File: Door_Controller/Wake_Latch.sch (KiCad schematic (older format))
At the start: 21 parts

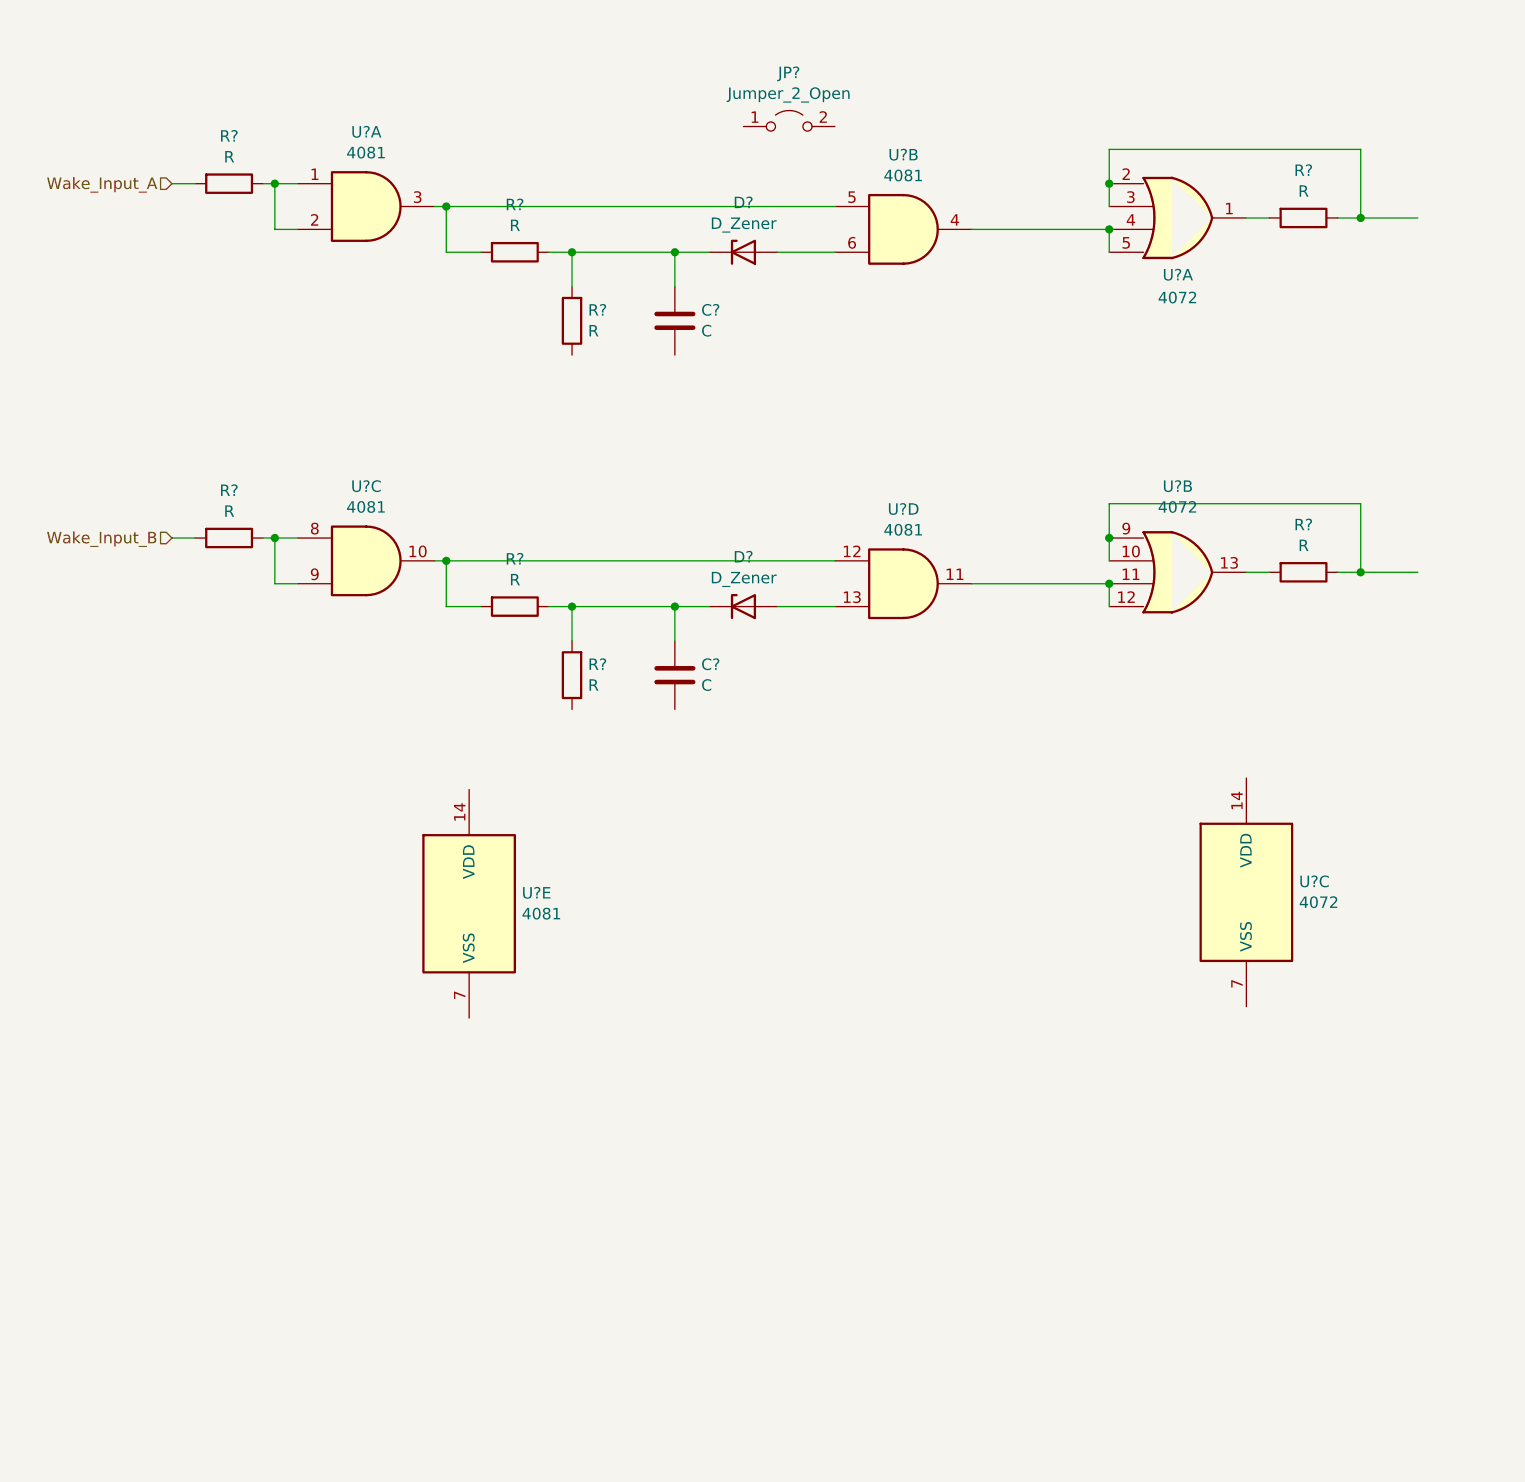
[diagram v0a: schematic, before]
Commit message: complete wake-latch subsheet
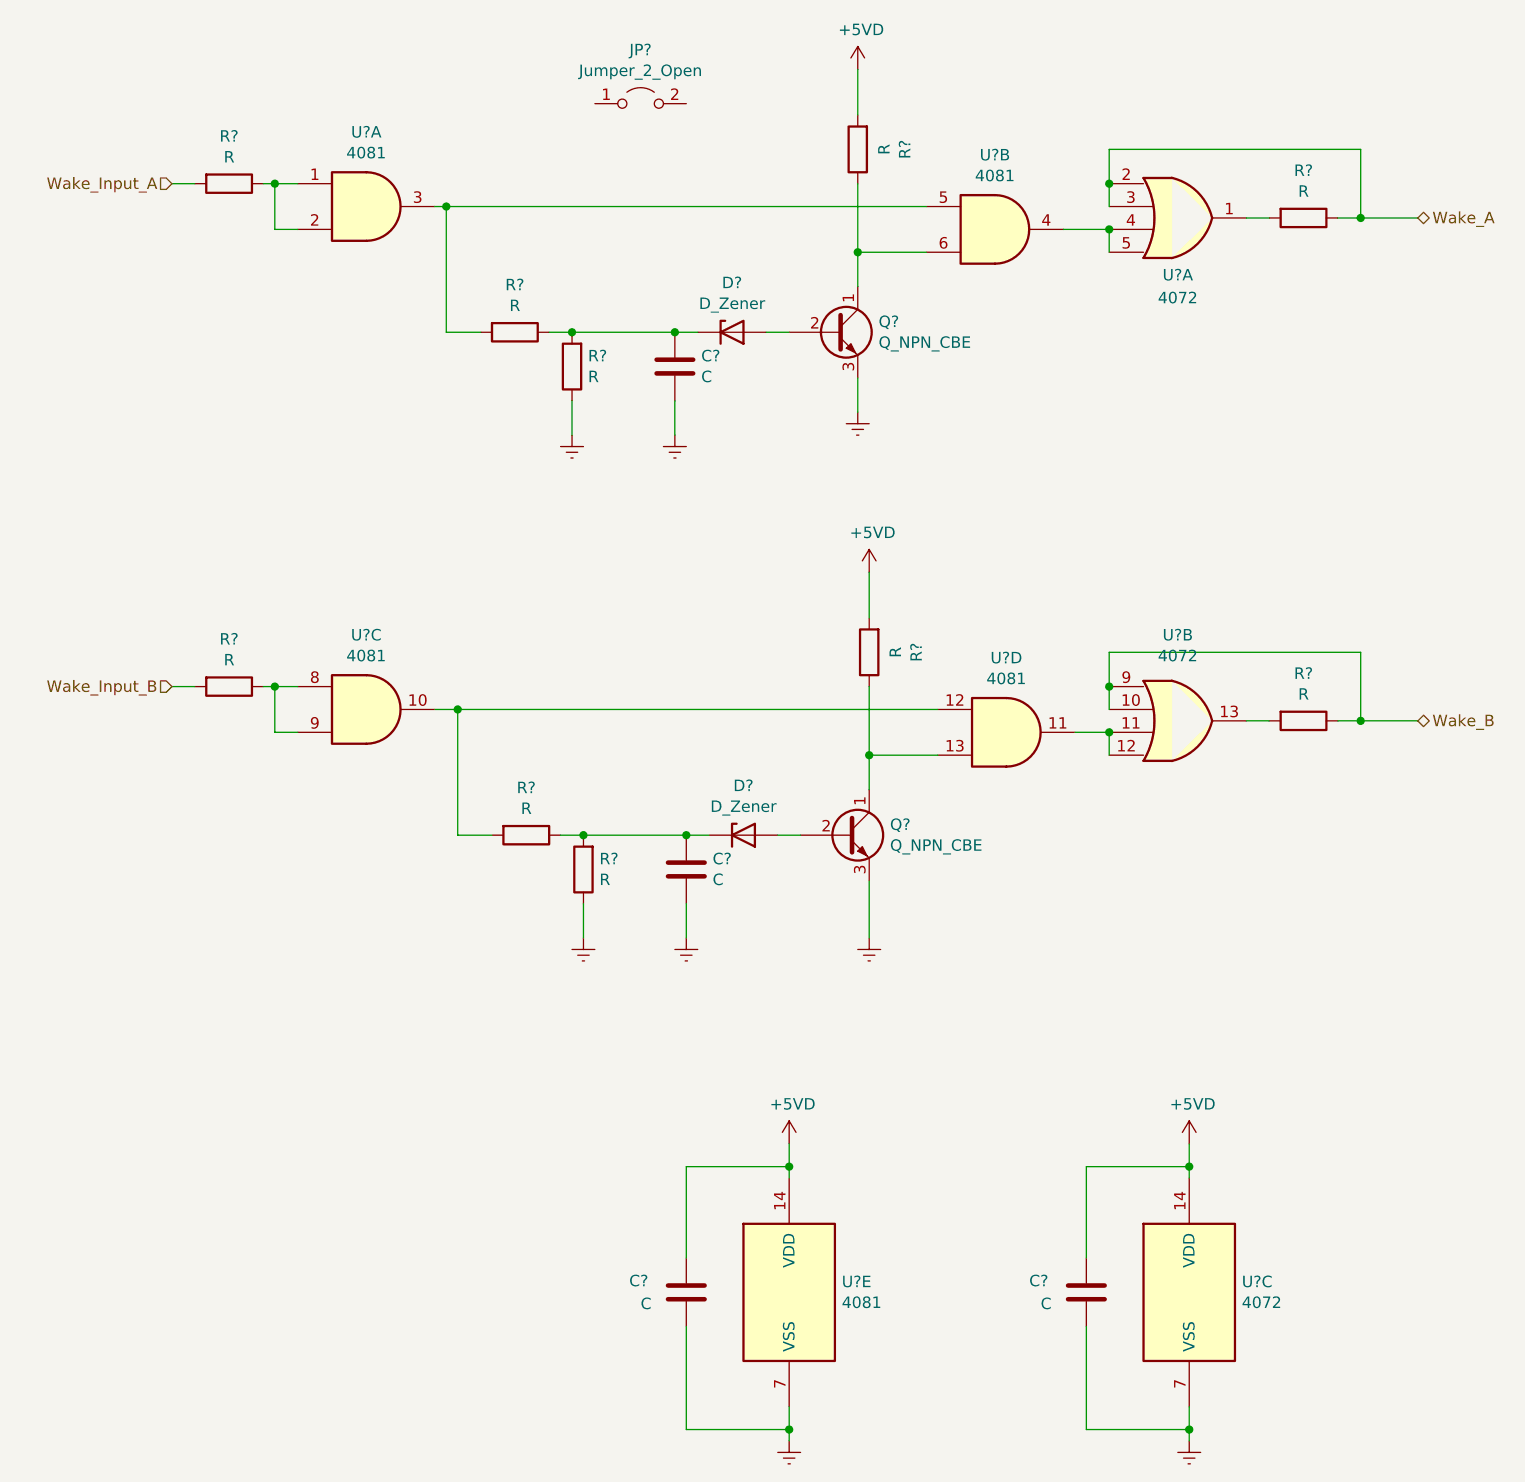
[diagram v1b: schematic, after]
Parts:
- removed C?: C, symbol Device:C
- removed D?: D_Zener, symbol Device:D_Zener
- removed R? (x2): R, symbol Device:R
- added C? (x3): C, symbol Device:C
- added D?: D_Zener, symbol Device:D_Zener
- added Q? (x2): Q_NPN_CBE, symbol Device:Q_NPN_CBE
- added R? (x4): R, symbol Device:R
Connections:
- net labels added: +5VD, Earth, Wake_A, Wake_B
- wire segments 48 -> 74
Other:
- moved on the sheet: C?, D?, JP?, R?, U?B, U?C, U?D, U?E

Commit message: simplified wake disable
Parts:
- removed JP?: Jumper_2_Open, symbol Jumper:Jumper_2_Open
- removed R? (x2): R, symbol Device:R
- R? (x2): value R -> 100
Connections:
- net Wake_A: now also U?.1; no longer U?.2, U?.3
- net Wake_B: now also U?.13; no longer U?.10, U?.9
- no-connect marks 0 -> 4
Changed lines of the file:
@@
 AR Path="/60BD8BC8/613ABD4B/60BF2346" Ref="R?"  Part="1"
 AR Path="/60BD8BC8/613AC461/60BF2346" Ref="R?"  Part="1"
-F 0 "R?" V 1343 1850 50  0000 C CNN
-F 1 "R" V 1434 1850 50  0000 C CNN
+F 0 "R?" V 1450 1850 50  0000 C CNN
+F 1 "100" V 1550 1850 50  0000 C CNN
 F 2 "" V 1480 1850 50  0001 C CNN
 F 3 "~" H 1550 1850 50  0001 C CNN
@@
 AR Path="/60BD8BC8/613ABD4B/60C15BD1" Ref="R?"  Part="1"
 AR Path="/60BD8BC8/613AC461/60C15BD1" Ref="R?"  Part="1"
-F 0 "R?" V 1343 4050 50  0000 C CNN
-F 1 "R" V 1434 4050 50  0000 C CNN
+F 0 "R?" V 1450 4050 50  0000 C CNN
+F 1 "100" V 1550 4050 50  0000 C CNN
 F 2 "" V 1480 4050 50  0001 C CNN
 F 3 "~" H 1550 4050 50  0001 C CNN
@@
 Wire Wire Line
 	1750 4050 1850 4050
-$Comp
-L Device:R R?
-U 1 1 60C216FA
-P 6250 4200
-AR Path="/60BD8BC8/60BD8C71/60C216FA" Ref="R?"  Part="1"
-AR Path="/60BD8BC8/613ABD4B/60C216FA" Ref="R?"  Part="1"
-AR Path="/60BD8BC8/613AC461/60C216FA" Ref="R?"  Part="1"
-F 0 "R?" V 6043 4200 50  0000 C CNN
-F 1 "R" V 6134 4200 50  0000 C CNN
-F 2 "" V 6180 4200 50  0001 C CNN
-F 3 "~" H 6250 4200 50  0001 C CNN
-	1    6250 4200
-	0    1    1    0
-$EndComp
-Wire Wire Line
-	6000 4200 6100 4200
-Wire Wire Line
-	6400 4200 6500 4200
-Wire Wire Line
-	6500 4200 6500 3900
-Wire Wire Line
-	6500 3900 5400 3900
-Connection ~ 6500 4200
-Wire Wire Line
-	6500 4200 6750 4200
-Wire Wire Line
-	5400 3900 5400 4050
-Wire Wire Line
-	5400 4050 5400 4150
-Connection ~ 5400 4050
 Wire Wire Line
 	5400 4250 5400 4350
@@
 	5400 4250 5250 4250
 Connection ~ 5400 4250
-$Comp
-L Jumper:Jumper_2_Open JP?
-U 1 1 60BECC23
-P 3350 1500
-AR Path="/60BD8BC8/60BD8C71/60BECC23" Ref="JP?"  Part="1"
-AR Path="/60BD8BC8/613ABD4B/60BECC23" Ref="JP?"  Part="1"
-AR Path="/60BD8BC8/613AC461/60BECC23" Ref="JP?"  Part="1"
-F 0 "JP?" H 3350 1735 50  0000 C CNN
-F 1 "Jumper_2_Open" H 3350 1644 50  0000 C CNN
-F 2 "" H 3350 1500 50  0001 C CNN
-F 3 "~" H 3350 1500 50  0001 C CNN
-	1    3350 1500
-	1    0    0    -1
-$EndComp
-Wire Wire Line
-	6500 2000 6750 2000
-Connection ~ 6500 2000
-Wire Wire Line
-	6500 2000 6500 1700
-Wire Wire Line
-	6000 2000 6100 2000
-$Comp
-L Device:R R?
-U 1 1 60C04CFC
-P 6250 2000
-AR Path="/60BD8BC8/60BD8C71/60C04CFC" Ref="R?"  Part="1"
-AR Path="/60BD8BC8/613ABD4B/60C04CFC" Ref="R?"  Part="1"
-AR Path="/60BD8BC8/613AC461/60C04CFC" Ref="R?"  Part="1"
-F 0 "R?" V 6043 2000 50  0000 C CNN
-F 1 "R" V 6134 2000 50  0000 C CNN
-F 2 "" V 6180 2000 50  0001 C CNN
-F 3 "~" H 6250 2000 50  0001 C CNN
-	1    6250 2000
-	0    1    1    0
-$EndComp
-Connection ~ 5400 1850
-Wire Wire Line
-	5400 1700 5400 1850
-Wire Wire Line
-	5400 1950 5400 1850
 Connection ~ 5400 2050
 Wire Wire Line
@@
 $EndComp
 Wire Wire Line
-	6400 2000 6500 2000
-Wire Wire Line
-	6500 1700 5400 1700
-Wire Wire Line
 	5200 2050 5400 2050
 $Comp
@@
 AR Path="/60BD8BC8/613ABD4B/6134AFF9" Ref="R?"  Part="1"
 AR Path="/60BD8BC8/613AC461/6134AFF9" Ref="R?"  Part="1"
-F 0 "R?" V 4093 1700 50  0000 C CNN
-F 1 "R" V 4184 1700 50  0000 C CNN
+F 0 "R?" V 4200 1700 50  0000 C CNN
+F 1 "R" V 4300 1700 50  0000 C CNN
 F 2 "" V 4230 1700 50  0001 C CNN
 F 3 "~" H 4300 1700 50  0001 C CNN
@@
 AR Path="/60BD8BC8/613ABD4B/61358B50" Ref="R?"  Part="1"
 AR Path="/60BD8BC8/613AC461/61358B50" Ref="R?"  Part="1"
-F 0 "R?" V 4143 3900 50  0000 C CNN
-F 1 "R" V 4234 3900 50  0000 C CNN
+F 0 "R?" V 4250 3900 50  0000 C CNN
+F 1 "R" V 4350 3900 50  0000 C CNN
 F 2 "" V 4280 3900 50  0001 C CNN
 F 3 "~" H 4350 3900 50  0001 C CNN
@@
 AR Path="/60BD8BC8/613ABD4B/60BF7A25" Ref="R?"  Part="1"
 AR Path="/60BD8BC8/613AC461/60BF7A25" Ref="R?"  Part="1"
-F 0 "R?" H 2980 2604 50  0000 R CNN
-F 1 "R" H 2980 2695 50  0000 R CNN
+F 0 "R?" V 2950 2700 50  0000 R CNN
+F 1 "R" V 3050 2700 50  0000 R CNN
 F 2 "" V 2980 2650 50  0001 C CNN
 F 3 "~" H 3050 2650 50  0001 C CNN
@@
 AR Path="/60BD8BC8/613ABD4B/60BF7586" Ref="R?"  Part="1"
 AR Path="/60BD8BC8/613AC461/60BF7586" Ref="R?"  Part="1"
-F 0 "R?" V 2593 2500 50  0000 C CNN
-F 1 "R" V 2684 2500 50  0000 C CNN
+F 0 "R?" V 2700 2500 50  0000 C CNN
+F 1 "R" V 2800 2500 50  0000 C CNN
 F 2 "" V 2730 2500 50  0001 C CNN
 F 3 "~" H 2800 2500 50  0001 C CNN
@@
 AR Path="/60BD8BC8/613ABD4B/613638AF" Ref="R?"  Part="1"
 AR Path="/60BD8BC8/613AC461/613638AF" Ref="R?"  Part="1"
-F 0 "R?" H 3030 4804 50  0000 R CNN
-F 1 "R" H 3030 4895 50  0000 R CNN
+F 0 "R?" V 3000 4900 50  0000 R CNN
+F 1 "R" V 3100 4900 50  0000 R CNN
 F 2 "" V 3030 4850 50  0001 C CNN
 F 3 "~" H 3100 4850 50  0001 C CNN
@@
 AR Path="/60BD8BC8/613ABD4B/613638B9" Ref="R?"  Part="1"
 AR Path="/60BD8BC8/613AC461/613638B9" Ref="R?"  Part="1"
-F 0 "R?" V 2643 4700 50  0000 C CNN
-F 1 "R" V 2734 4700 50  0000 C CNN
+F 0 "R?" V 2750 4700 50  0000 C CNN
+F 1 "R" V 2850 4700 50  0000 C CNN
 F 2 "" V 2780 4700 50  0001 C CNN
 F 3 "~" H 2850 4700 50  0001 C CNN
@@
 Text HLabel 6750 4200 2    50   BiDi ~ 0
 Wake_B
+Wire Wire Line
+	6000 2000 6750 2000
+NoConn ~ 5400 1850
+NoConn ~ 5400 1950
+NoConn ~ 5400 4050
+NoConn ~ 5400 4150
+Wire Wire Line
+	6000 4200 6750 4200
 $EndSCHEMATC

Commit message: specify wake pulse circuit to ltspice model
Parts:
- C? (x2): value C -> 220nF
- D? (x2): value D_Zener -> 4.7V
- R? (x4): value R -> 100K
- R? (x2): value R -> 1M
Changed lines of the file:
@@
 AR Path="/60BD8BC8/613AC461/6134AFF9" Ref="R?"  Part="1"
 F 0 "R?" V 4200 1700 50  0000 C CNN
-F 1 "R" V 4300 1700 50  0000 C CNN
+F 1 "100K" V 4300 1700 50  0000 C CNN
 F 2 "" V 4230 1700 50  0001 C CNN
 F 3 "~" H 4300 1700 50  0001 C CNN
@@
 AR Path="/60BD8BC8/613AC461/61358B50" Ref="R?"  Part="1"
 F 0 "R?" V 4250 3900 50  0000 C CNN
-F 1 "R" V 4350 3900 50  0000 C CNN
+F 1 "100K" V 4350 3900 50  0000 C CNN
 F 2 "" V 4280 3900 50  0001 C CNN
 F 3 "~" H 4350 3900 50  0001 C CNN
@@
 AR Path="/60BD8BC8/613AC461/60BFAC12" Ref="D?"  Part="1"
 F 0 "D?" H 3750 2716 50  0000 C CNN
-F 1 "D_Zener" H 3750 2625 50  0000 C CNN
+F 1 "4.7V" H 3750 2625 50  0000 C CNN
 F 2 "" H 3750 2500 50  0001 C CNN
 F 3 "~" H 3750 2500 50  0001 C CNN
@@
 AR Path="/60BD8BC8/613AC461/60BF9FE4" Ref="C?"  Part="1"
 F 0 "C?" H 3615 2696 50  0000 L CNN
-F 1 "C" H 3615 2605 50  0000 L CNN
+F 1 "220nF" H 3615 2605 50  0000 L CNN
 F 2 "" H 3538 2500 50  0001 C CNN
 F 3 "~" H 3500 2650 50  0001 C CNN
@@
 AR Path="/60BD8BC8/613AC461/60BF7A25" Ref="R?"  Part="1"
 F 0 "R?" V 2950 2700 50  0000 R CNN
-F 1 "R" V 3050 2700 50  0000 R CNN
+F 1 "1M" V 3050 2700 50  0000 R CNN
 F 2 "" V 2980 2650 50  0001 C CNN
 F 3 "~" H 3050 2650 50  0001 C CNN
@@
 AR Path="/60BD8BC8/613AC461/60BF7586" Ref="R?"  Part="1"
 F 0 "R?" V 2700 2500 50  0000 C CNN
-F 1 "R" V 2800 2500 50  0000 C CNN
+F 1 "100K" V 2800 2500 50  0000 C CNN
 F 2 "" V 2730 2500 50  0001 C CNN
 F 3 "~" H 2800 2500 50  0001 C CNN
@@
 AR Path="/60BD8BC8/613AC461/6136389B" Ref="D?"  Part="1"
 F 0 "D?" H 3800 4916 50  0000 C CNN
-F 1 "D_Zener" H 3800 4825 50  0000 C CNN
+F 1 "4.7V" H 3800 4825 50  0000 C CNN
 F 2 "" H 3800 4700 50  0001 C CNN
 F 3 "~" H 3800 4700 50  0001 C CNN
@@
 AR Path="/60BD8BC8/613AC461/613638A5" Ref="C?"  Part="1"
 F 0 "C?" H 3665 4896 50  0000 L CNN
-F 1 "C" H 3665 4805 50  0000 L CNN
+F 1 "220nF" H 3665 4805 50  0000 L CNN
 F 2 "" H 3588 4700 50  0001 C CNN
 F 3 "~" H 3550 4850 50  0001 C CNN
@@
 AR Path="/60BD8BC8/613AC461/613638AF" Ref="R?"  Part="1"
 F 0 "R?" V 3000 4900 50  0000 R CNN
-F 1 "R" V 3100 4900 50  0000 R CNN
+F 1 "1M" V 3100 4900 50  0000 R CNN
 F 2 "" V 3030 4850 50  0001 C CNN
 F 3 "~" H 3100 4850 50  0001 C CNN
@@
 AR Path="/60BD8BC8/613AC461/613638B9" Ref="R?"  Part="1"
 F 0 "R?" V 2750 4700 50  0000 C CNN
-F 1 "R" V 2850 4700 50  0000 C CNN
+F 1 "100K" V 2850 4700 50  0000 C CNN
 F 2 "" V 2780 4700 50  0001 C CNN
 F 3 "~" H 2850 4700 50  0001 C CNN
